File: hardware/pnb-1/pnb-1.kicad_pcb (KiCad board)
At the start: 2 copper layers, 58 x 42 mm, 37 parts, among them J1 USB-C 16P, J3 DTR 2x6 DNP, J4 UART 1x4, SW1 BOOT, SW2 RESET, U1 ESP32-S3-MINI-1-N8, U2 AMS1117-3.3, U3 SCD41-D-R2, U4 BH1750FVI-TR

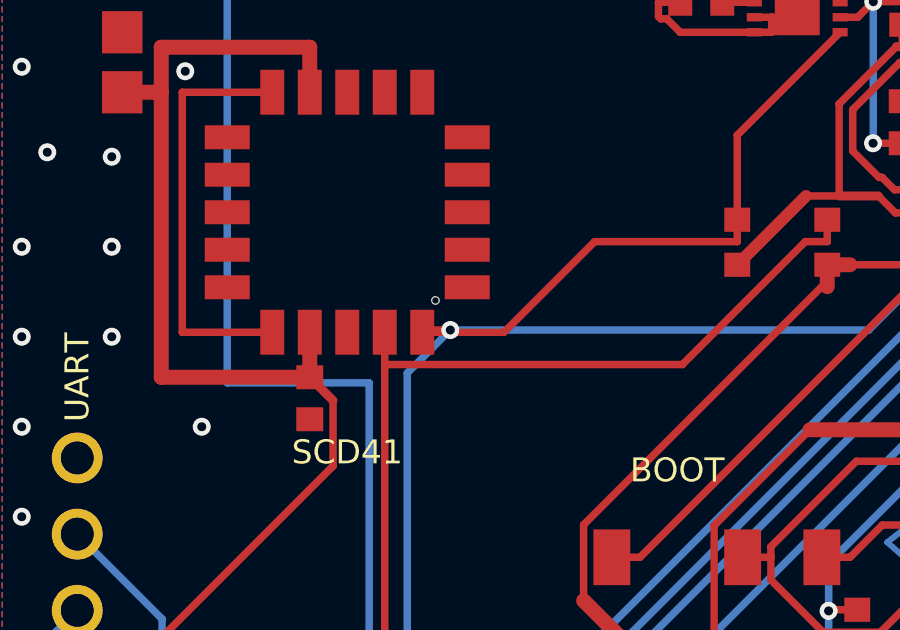
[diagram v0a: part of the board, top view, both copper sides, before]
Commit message: fix(pcb): meet JLCPCB NPTH clearance
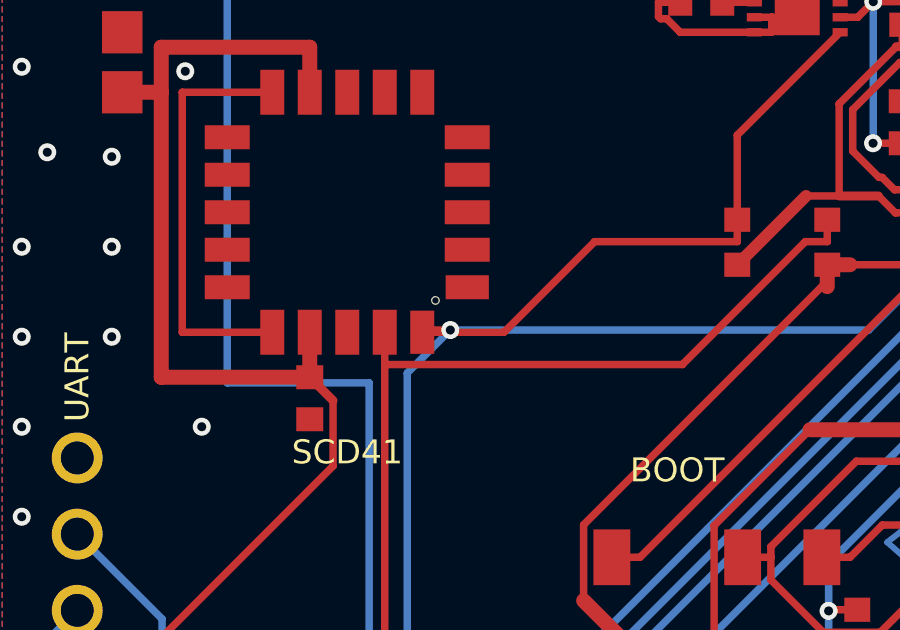
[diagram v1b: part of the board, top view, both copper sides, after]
